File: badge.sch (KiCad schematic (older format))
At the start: 42 parts, among them U1 TPS61165

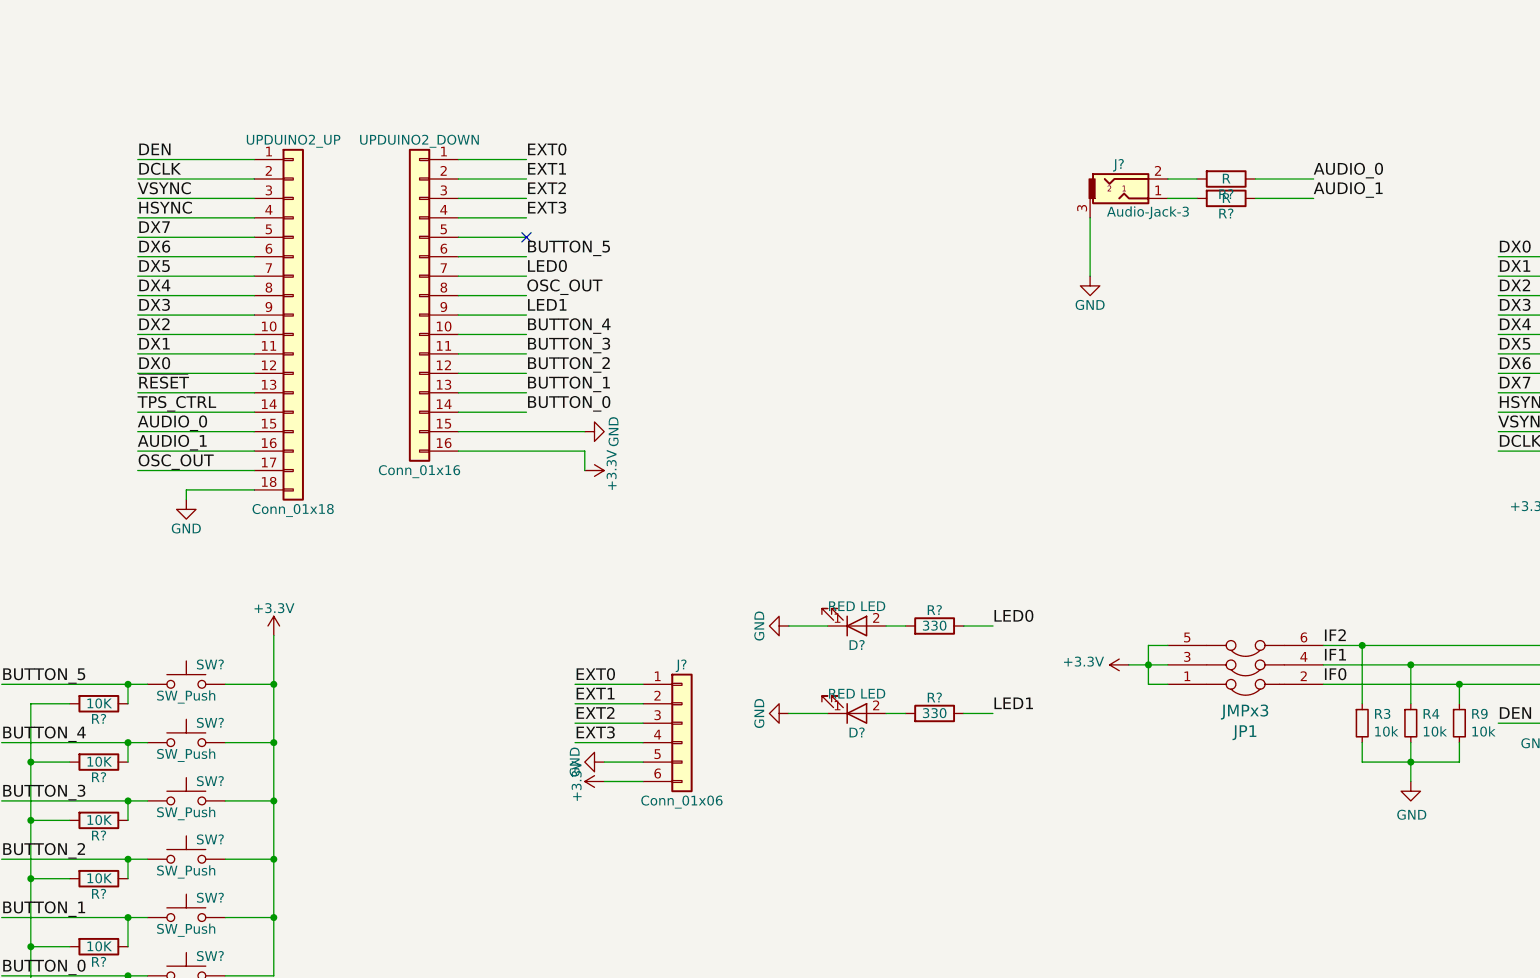
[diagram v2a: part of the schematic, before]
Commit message: Made audio mono and using pin 37, change port to PMOD, clk on proper pin,
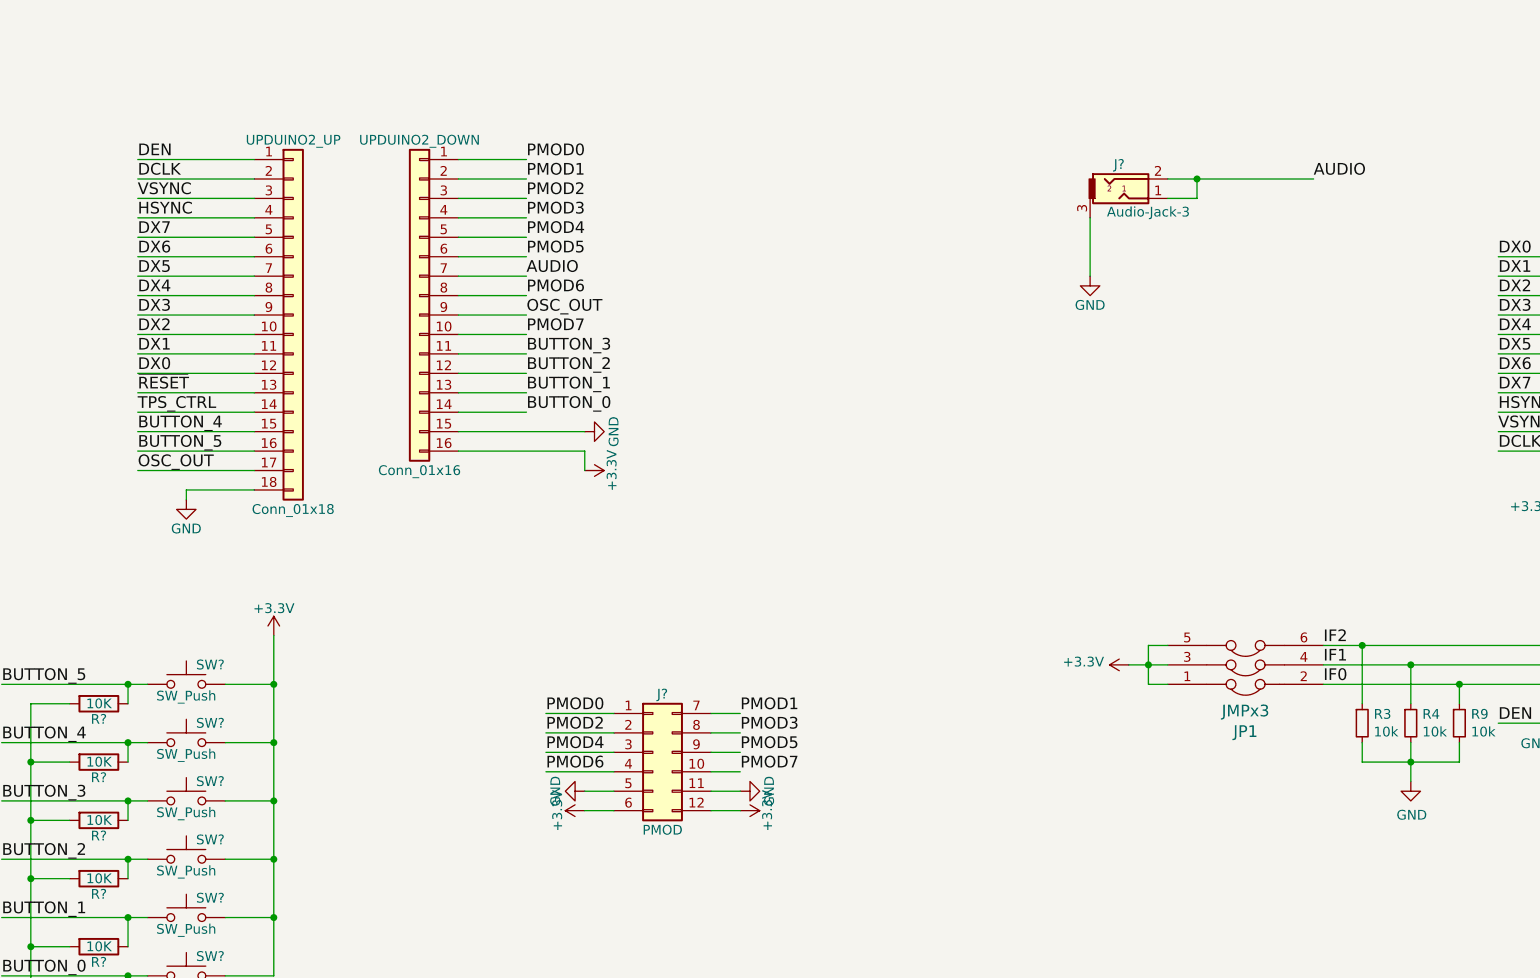
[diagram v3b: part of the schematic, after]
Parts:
- removed D? (x2): RED LED, symbol LED
- removed J?: Conn_01x06, symbol Conn_01x06
- removed R? (x2): R, symbol R
- removed R? (x2): 330, symbol R
- added J?: PMOD, symbol Conn_02x06_Top_Bottom
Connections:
- net AUDIO_0 is gone; now on net BUTTON_4: UPDUINO2_UP.15 (Pin_15)
- net AUDIO_1 is gone; now on net BUTTON_5: UPDUINO2_UP.16 (Pin_16)
- net LED0 is gone; now on net AUDIO: UPDUINO2_DOWN.7 (Pin_7)
- net LED1 is gone; now on net OSC_OUT: UPDUINO2_DOWN.9 (Pin_9)
- net +3V3: now also J?.12 (Pin_12), J?.6 (Pin_6)
- net BUTTON_4: no longer UPDUINO2_DOWN.10 (Pin_10)
- net BUTTON_5: no longer UPDUINO2_DOWN.6 (Pin_6)
- net GND: now also J?.11 (Pin_11), J?.5 (Pin_5)
- net OSC_OUT: no longer UPDUINO2_DOWN.8 (Pin_8)
- net PMOD4: now reaches UPDUINO2_DOWN.5 (Pin_5)
- net PMOD4: now also J?.3 (Pin_3)
- net AUDIO: now reaches J?.1
- net AUDIO: now also J?.2
- net EXT0 renamed PMOD0
- net PMOD0: now also J?.1 (Pin_1)
- net EXT1 renamed PMOD1
- net PMOD1: now also J?.7 (Pin_7)
- net EXT2 renamed PMOD2
- net PMOD2: now also J?.2 (Pin_2)
- net EXT3 renamed PMOD3
- net PMOD3: now also J?.8 (Pin_8)
- new net PMOD5: J?.9 (Pin_9), UPDUINO2_DOWN.6 (Pin_6)
- new net PMOD6: J?.4 (Pin_4), UPDUINO2_DOWN.8 (Pin_8)
- new net PMOD7: J?.10 (Pin_10), UPDUINO2_DOWN.10 (Pin_10)
- no-connect marks 12 -> 11
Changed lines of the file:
@@
 DEN
 Text Label 5900 6200 0    60   ~ 0
-AUDIO_1
+BUTTON_5
 Text Label 5900 6100 0    60   ~ 0
-AUDIO_0
+BUTTON_4
 Text Label 5900 6000 0    60   ~ 0
 TPS_CTRL
@@
 $EndComp
 Text Label 11950 4800 0    60   ~ 0
-AUDIO_0
+AUDIO
 Text Label 7900 4700 0    60   ~ 0
-EXT0
+PMOD0
 Text Label 7900 4800 0    60   ~ 0
-EXT1
-Text Label 11950 4900 0    60   ~ 0
-AUDIO_1
+PMOD1
 Text Label 7900 6000 0    60   ~ 0
 BUTTON_0
@@
 BUTTON_3
 Text Label 7900 5600 0    60   ~ 0
-BUTTON_4
+PMOD7
 $Comp
 L SW_Push SW?
@@
 $EndComp
 $Comp
-L R R?
-U 1 1 5A7F4132
-P 11500 4800
-F 0 "R?" V 11580 4800 50  0000 C CNN
-F 1 "R" V 11500 4800 50  0000 C CNN
-F 2 "" V 11430 4800 50  0001 C CNN
-F 3 "" H 11500 4800 50  0001 C CNN
-	1    11500 4800
-	0    1    1    0
-$EndComp
-$Comp
-L R R?
-U 1 1 5A7F41B1
-P 11500 4900
-F 0 "R?" V 11580 4900 50  0000 C CNN
-F 1 "R" V 11500 4900 50  0000 C CNN
-F 2 "" V 11430 4900 50  0001 C CNN
-F 3 "" H 11500 4900 50  0001 C CNN
-	1    11500 4900
-	0    1    1    0
-$EndComp
-$Comp
 L Audio-Jack-3 J?
 U 1 1 5A7F3EF2
@@
 	1    0    0    -1
 $EndComp
-Text Label 8150 7400 0    60   ~ 0
-EXT0
-Text Label 8150 7500 0    60   ~ 0
-EXT1
-Text Label 8150 7600 0    60   ~ 0
-EXT2
 Text Label 7900 4900 0    60   ~ 0
-EXT2
+PMOD2
 Text Label 7900 5000 0    60   ~ 0
-EXT3
-Text Label 7900 5200 0    60   ~ 0
-BUTTON_5
+PMOD3
 Text Label 7900 5400 0    60   ~ 0
-OSC_OUT
+PMOD6
 $Comp
 L GND #PWR?
@@
 	1    0    0    -1
 $EndComp
-$Comp
-L LED D?
-U 1 1 5A7FC771
-P 9600 7100
-F 0 "D?" H 9600 7200 50  0000 C CNN
-F 1 "RED LED" H 9600 7000 50  0000 C CNN
-F 2 "" H 9600 7100 50  0001 C CNN
-F 3 "" H 9600 7100 50  0001 C CNN
-	1    9600 7100
-	1    0    0    1
-$EndComp
-$Comp
-L R R?
-U 1 1 5A7FC9C8
-P 10000 7100
-F 0 "R?" V 10080 7100 50  0000 C CNN
-F 1 "330" V 10000 7100 50  0000 C CNN
-F 2 "" V 9930 7100 50  0001 C CNN
-F 3 "" H 10000 7100 50  0001 C CNN
-	1    10000 7100
-	0    1    -1   0
-$EndComp
-Text Label 10300 7100 0    60   ~ 0
-LED0
-$Comp
-L GND #PWR?
-U 1 1 5A7FCB50
-P 9250 7100
-F 0 "#PWR?" H 9250 6850 50  0001 C CNN
-F 1 "GND" H 9250 6950 50  0000 C CNN
-F 2 "" H 9250 7100 50  0001 C CNN
-F 3 "" H 9250 7100 50  0001 C CNN
-	1    9250 7100
-	0    1    -1   0
-$EndComp
 Wire Wire Line
 	6150 6400 6500 6400
@@
 	6150 6450 6150 6400
 Wire Wire Line
-	8150 7600 8500 7600
-Wire Wire Line
-	8150 7500 8500 7500
-Wire Wire Line
-	8150 7400 8500 7400
-Wire Wire Line
 	7550 5400 7900 5400
 Wire Wire Line
@@
 Wire Wire Line
 	7550 4900 7900 4900
-Wire Wire Line
-	11650 4900 11950 4900
 Wire Wire Line
 	11200 4900 11350 4900
@@
 Connection ~ 5850 8900
 Wire Wire Line
-	11200 4800 11350 4800
-Wire Wire Line
-	11650 4800 11950 4800
-Wire Wire Line
-	9450 7100 9250 7100
-Wire Wire Line
-	10300 7100 10150 7100
-Wire Wire Line
-	9850 7100 9750 7100
+	11200 4800 11950 4800
 $Comp
 L Conn_01x02 BATTERY
@@
 Wire Wire Line
 	6750 3600 6850 3600
-Text Label 8150 7700 0    60   ~ 0
-EXT3
-Wire Wire Line
-	8150 7700 8500 7700
-$Comp
-L Conn_01x06 J?
-U 1 1 5A7F0509
-P 8700 7600
-F 0 "J?" H 8700 7900 50  0000 C CNN
-F 1 "Conn_01x06" H 8700 7200 50  0000 C CNN
-F 2 "" H 8700 7600 50  0001 C CNN
-F 3 "" H 8700 7600 50  0001 C CNN
-	1    8700 7600
-	1    0    0    -1
-$EndComp
-$Comp
-L GND #PWR?
-U 1 1 5A7F0582
-P 8300 7800
-F 0 "#PWR?" H 8300 7550 50  0001 C CNN
-F 1 "GND" H 8300 7650 50  0000 C CNN
-F 2 "" H 8300 7800 50  0001 C CNN
-F 3 "" H 8300 7800 50  0001 C CNN
-	1    8300 7800
-	0    1    1    0
-$EndComp
-$Comp
-L +3.3V #PWR?
-U 1 1 5A7F0636
-P 8300 7900
-F 0 "#PWR?" H 8300 7750 50  0001 C CNN
-F 1 "+3.3V" H 8300 8040 50  0000 C CNN
-F 2 "" H 8300 7900 50  0001 C CNN
-F 3 "" H 8300 7900 50  0001 C CNN
-	1    8300 7900
-	0    -1   -1   0
-$EndComp
-Wire Wire Line
-	8300 7800 8500 7800
-Wire Wire Line
-	8300 7900 8500 7900
 Wire Wire Line
 	13450 3300 12800 3300
@@
 Wire Wire Line
 	13450 3500 12800 3500
-Text Label 7900 5300 0    60   ~ 0
-LED0
 Text Label 7900 5500 0    60   ~ 0
-LED1
+OSC_OUT
 Wire Wire Line
 	7900 5300 7550 5300
 Wire Wire Line
 	7900 5500 7550 5500
-$Comp
-L LED D?
-U 1 1 5A7F8496
-P 9600 7550
-F 0 "D?" H 9600 7650 50  0000 C CNN
-F 1 "RED LED" H 9600 7450 50  0000 C CNN
-F 2 "" H 9600 7550 50  0001 C CNN
-F 3 "" H 9600 7550 50  0001 C CNN
-	1    9600 7550
-	1    0    0    1
-$EndComp
-$Comp
-L R R?
-U 1 1 5A7F849C
-P 10000 7550
-F 0 "R?" V 10080 7550 50  0000 C CNN
-F 1 "330" V 10000 7550 50  0000 C CNN
-F 2 "" V 9930 7550 50  0001 C CNN
-F 3 "" H 10000 7550 50  0001 C CNN
-	1    10000 7550
-	0    1    -1   0
-$EndComp
-Text Label 10300 7550 0    60   ~ 0
-LED1
-$Comp
-L GND #PWR?
-U 1 1 5A7F84A3
-P 9250 7550
-F 0 "#PWR?" H 9250 7300 50  0001 C CNN
-F 1 "GND" H 9250 7400 50  0000 C CNN
-F 2 "" H 9250 7550 50  0001 C CNN
-F 3 "" H 9250 7550 50  0001 C CNN
-	1    9250 7550
-	0    1    -1   0
-$EndComp
-Wire Wire Line
-	9450 7550 9250 7550
-Wire Wire Line
-	10300 7550 10150 7550
-Wire Wire Line
-	9850 7550 9750 7550
 Text Label 8750 1800 0    60   ~ 0
 TPS_CTRL
@@
 	8450 1800 8450 1600
 Connection ~ 8450 1600
-NoConn ~ 7900 5100
 NoConn ~ 7250 3700
+Text Label 7900 5100 0    60   ~ 0
+PMOD4
+Text Label 7900 5200 0    60   ~ 0
+PMOD5
+Text Label 7900 5300 0    60   ~ 0
+AUDIO
+Wire Wire Line
+	11350 4900 11350 4800
+Connection ~ 11350 4800
+$Comp
+L Conn_02x06_Top_Bottom J?
+U 1 1 5A7F4E92
+P 8550 7750
+F 0 "J?" H 8600 8050 50  0000 C CNN
+F 1 "PMOD" H 8600 7350 50  0000 C CNN
+F 2 "" H 8550 7750 50  0001 C CNN
+F 3 "" H 8550 7750 50  0001 C CNN
+	1    8550 7750
+	1    0    0    -1
+$EndComp
+$Comp
+L GND #PWR?
+U 1 1 5A7F4F71
+P 8200 7950
+F 0 "#PWR?" H 8200 7700 50  0001 C CNN
+F 1 "GND" H 8200 7800 50  0000 C CNN
+F 2 "" H 8200 7950 50  0001 C CNN
+F 3 "" H 8200 7950 50  0001 C CNN
+	1    8200 7950
+	0    1    1    0
+$EndComp
+$Comp
+L GND #PWR?
+U 1 1 5A7F501C
+P 9000 7950
+F 0 "#PWR?" H 9000 7700 50  0001 C CNN
+F 1 "GND" H 9000 7800 50  0000 C CNN
+F 2 "" H 9000 7950 50  0001 C CNN
+F 3 "" H 9000 7950 50  0001 C CNN
+	1    9000 7950
+	0    -1   -1   0
+$EndComp
+$Comp
+L +3.3V #PWR?
+U 1 1 5A7F5078
+P 8200 8050
+F 0 "#PWR?" H 8200 7900 50  0001 C CNN
+F 1 "+3.3V" H 8200 8190 50  0000 C CNN
+F 2 "" H 8200 8050 50  0001 C CNN
+F 3 "" H 8200 8050 50  0001 C CNN
+	1    8200 8050
+	0    -1   -1   0
+$EndComp
+$Comp
+L +3.3V #PWR?
+U 1 1 5A7F514A
+P 9000 8050
+F 0 "#PWR?" H 9000 7900 50  0001 C CNN
+F 1 "+3.3V" H 9000 8190 50  0000 C CNN
+F 2 "" H 9000 8050 50  0001 C CNN
+F 3 "" H 9000 8050 50  0001 C CNN
+	1    9000 8050
+	0    1    1    0
+$EndComp
+Wire Wire Line
+	9000 8050 8850 8050
+Wire Wire Line
+	8350 7950 8200 7950
+Wire Wire Line
+	8350 8050 8200 8050
+Wire Wire Line
+	8850 7950 9000 7950
+Text Label 8000 7550 0    60   ~ 0
+PMOD0
+Text Label 8000 7650 0    60   ~ 0
+PMOD2
+Text Label 8000 7750 0    60   ~ 0
+PMOD4
+Text Label 8000 7850 0    60   ~ 0
+PMOD6
+Text Label 9000 7550 0    60   ~ 0
+PMOD1
+Text Label 9000 7650 0    60   ~ 0
+PMOD3
+Text Label 9000 7750 0    60   ~ 0
+PMOD5
+Text Label 9000 7850 0    60   ~ 0
+PMOD7
+Wire Wire Line
+	9000 7550 8850 7550
+Wire Wire Line
+	9000 7650 8850 7650
+Wire Wire Line
+	9000 7750 8850 7750
+Wire Wire Line
+	9000 7850 8850 7850
+Wire Wire Line
+	8000 7550 8350 7550
+Wire Wire Line
+	8000 7650 8350 7650
+Wire Wire Line
+	8000 7750 8350 7750
+Wire Wire Line
+	8000 7850 8350 7850
 $EndSCHEMATC

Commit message: Footprint assignments and initial placement
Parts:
- removed JP1: JMPx3, Pin_Headers:Pin_Header_Straight_2x03_Pitch2.54mm, symbol JMPx3
- added J3, J4: HOLE, Mounting_Holes:MountingHole_3.2mm_M3, symbol Conn_01x01
- added R16, R17: DNP, Resistors_SMD:R_0603, symbol R_Small
- added R18: 10k, Resistors_SMD:R_0603, symbol R_Small
- BATTERY1: renamed from BATTERY; footprint (none) -> Pin_Headers:Pin_Header_Straight_1x02_Pitch2.54mm
- J1: renamed from J?; footprint (none) -> Custom Parts:Pin_Header_Angled_2x06_Pitch2.54mm_PMOD
- J2: renamed from J?; footprint (none) -> Custom Parts:AUDIO_JACK_3.5mm
- R10, R11, R12, R13, R14, R15: renamed from R?; footprint (none) -> Resistors_SMD:R_0603
- R9: value 10k -> DNP
- SW1, SW2, SW3, SW4, SW5, SW6: renamed from SW?; footprint (none) -> Buttons_Switches_THT:SW_PUSH-12mm
- SW7: renamed from SW?; footprint (none) -> Buttons_Switches_THT:SW_CuK_OS102011MA1QN1_SPDT_Angled
- UPDUINO2_DOWN1: renamed from UPDUINO2_DOWN; footprint (none) -> Pin_Headers:Pin_Header_Straight_1x16_Pitch2.54mm
- UPDUINO2_UP1: renamed from UPDUINO2_UP; footprint (none) -> Pin_Headers:Pin_Header_Straight_1x18_Pitch2.54mm
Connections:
- net +3V3: now also R16.2, R17.2, R18.2
- net DCLK: now also UPDUINO2_UP1.12 (Pin_12); no longer UPDUINO2_UP1.2 (Pin_2)
- net DEN: now also UPDUINO2_UP1.13 (Pin_13); no longer UPDUINO2_UP1.1 (Pin_1)
- net DX0: now also UPDUINO2_UP1.2 (Pin_2); no longer UPDUINO2_UP1.12 (Pin_12)
- net DX1: now also UPDUINO2_UP1.3 (Pin_3); no longer UPDUINO2_UP1.11 (Pin_11)
- net DX2: now also UPDUINO2_UP1.4 (Pin_4); no longer UPDUINO2_UP1.10 (Pin_10)
- net DX3: now also UPDUINO2_UP1.5 (Pin_5); no longer UPDUINO2_UP1.9 (Pin_9)
- net DX4: now also UPDUINO2_UP1.6 (Pin_6); no longer UPDUINO2_UP1.8 (Pin_8)
- net DX6: now also UPDUINO2_UP1.8 (Pin_8); no longer UPDUINO2_UP1.6 (Pin_6)
- net DX7: now also UPDUINO2_UP1.9 (Pin_9); no longer UPDUINO2_UP1.5 (Pin_5)
- net HSYNC: now also UPDUINO2_UP1.10 (Pin_10); no longer UPDUINO2_UP1.4 (Pin_4)
- net IF0: now also R18.1
- net IF1: now also R17.1
- net IF2: now also R16.1
- net PMOD0: now also UPDUINO2_DOWN1.10 (Pin_10); no longer UPDUINO2_DOWN1.1 (Pin_1)
- net PMOD1: now also UPDUINO2_DOWN1.8 (Pin_8); no longer UPDUINO2_DOWN1.2 (Pin_2)
- net PMOD2: now also UPDUINO2_DOWN1.6 (Pin_6); no longer UPDUINO2_DOWN1.3 (Pin_3)
- net PMOD3: now also UPDUINO2_DOWN1.5 (Pin_5); no longer UPDUINO2_DOWN1.4 (Pin_4)
- net PMOD4: now also UPDUINO2_DOWN1.4 (Pin_4); no longer UPDUINO2_DOWN1.5 (Pin_5)
- net PMOD5: now also UPDUINO2_DOWN1.3 (Pin_3); no longer UPDUINO2_DOWN1.6 (Pin_6)
- net PMOD6: now also UPDUINO2_DOWN1.2 (Pin_2); no longer UPDUINO2_DOWN1.8 (Pin_8)
- net PMOD7: now also UPDUINO2_DOWN1.1 (Pin_1); no longer UPDUINO2_DOWN1.10 (Pin_10)
- net VSYNC: now also UPDUINO2_UP1.11 (Pin_11); no longer UPDUINO2_UP1.3 (Pin_3)
- net ~RESET: now also UPDUINO2_UP1.1 (Pin_1); no longer UPDUINO2_UP1.13 (Pin_13)
- no-connect marks 11 -> 13

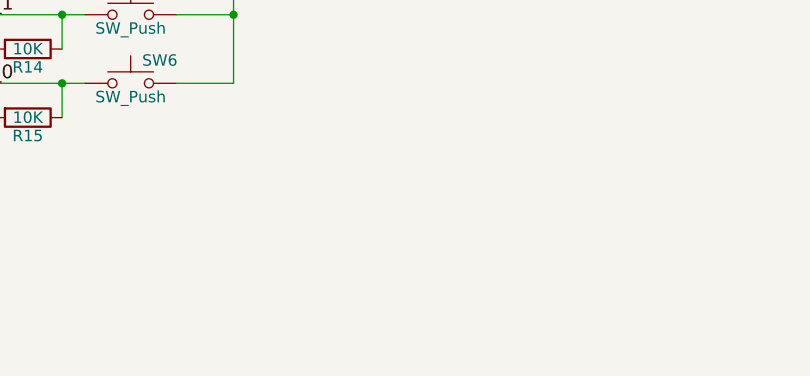
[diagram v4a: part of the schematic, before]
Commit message: Routing done and logos added
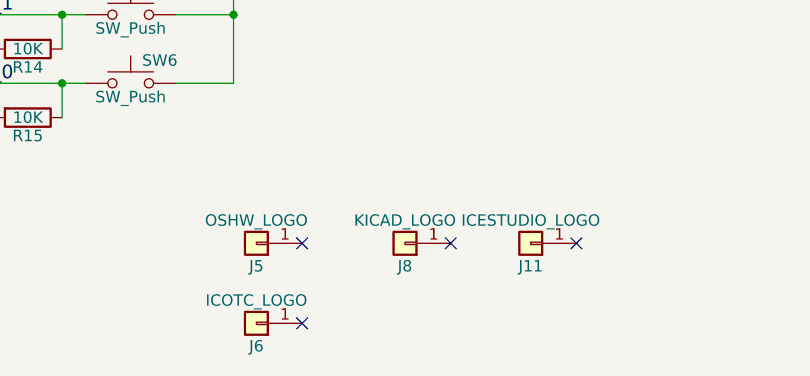
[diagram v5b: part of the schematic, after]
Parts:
- added J11: ICESTUDIO_LOGO, Custom Parts:ICESTUDIO, symbol Conn_01x01
- added J5: OSHW_LOGO, Symbols:OSHW-Logo2_24.3x20mm_SilkScreen, symbol Conn_01x01
- added J6: ICOTC_LOGO, Custom Parts:ICOTC, symbol Conn_01x01
- added J8: KICAD_LOGO, Symbols:KiCad-Logo_12mm_SilkScreen, symbol Conn_01x01
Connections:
- no-connect marks 13 -> 17
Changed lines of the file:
@@
 NoConn ~ 6350 2600
 NoConn ~ 6350 2900
+$Comp
+L Conn_01x01 J5
+U 1 1 5A80235E
+P 6700 9600
+F 0 "J5" H 6700 9700 50  0000 C CNN
+F 1 "OSHW_LOGO" H 6700 9500 50  0000 C CNN
+F 2 "Symbols:OSHW-Logo2_24.3x20mm_SilkScreen" H 6700 9600 50  0001 C CNN
+F 3 "" H 6700 9600 50  0001 C CNN
+	1    6700 9600
+	-1   0    0    1
+$EndComp
+NoConn ~ 6900 9600
+$Comp
+L Conn_01x01 J6
+U 1 1 5A802842
+P 6700 9950
+F 0 "J6" H 6700 10050 50  0000 C CNN
+F 1 "ICOTC_LOGO" H 6700 9850 50  0000 C CNN
+F 2 "Custom Parts:ICOTC" H 6700 9950 50  0001 C CNN
+F 3 "" H 6700 9950 50  0001 C CNN
+	1    6700 9950
+	-1   0    0    1
+$EndComp
+$Comp
+L Conn_01x01 J8
+U 1 1 5A802C1B
+P 7350 9600
+F 0 "J8" H 7350 9700 50  0000 C CNN
+F 1 "KICAD_LOGO" H 7350 9500 50  0000 C CNN
+F 2 "Symbols:KiCad-Logo_12mm_SilkScreen" H 7350 9600 50  0001 C CNN
+F 3 "" H 7350 9600 50  0001 C CNN
+	1    7350 9600
+	-1   0    0    1
+$EndComp
+NoConn ~ 7550 9600
+NoConn ~ 6900 9950
+$Comp
+L Conn_01x01 J11
+U 1 1 5A8032EC
+P 7900 9600
+F 0 "J11" H 7900 9700 50  0000 C CNN
+F 1 "ICESTUDIO_LOGO" H 7900 9500 50  0000 C CNN
+F 2 "Custom Parts:ICESTUDIO" H 7900 9600 50  0001 C CNN
+F 3 "" H 7900 9600 50  0001 C CNN
+	1    7900 9600
+	-1   0    0    1
+$EndComp
+NoConn ~ 8100 9600
 $EndSCHEMATC

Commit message: Final tweaks, create gerbers
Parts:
- added J7: OSHPARK_LOGO, Custom Parts:OSHPARK, symbol Conn_01x01
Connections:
- no-connect marks 17 -> 20
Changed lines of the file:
@@
 $EndComp
 NoConn ~ 8100 9600
+$Comp
+L Conn_01x01 J7
+U 1 1 5A81D496
+P 7350 9950
+F 0 "J7" H 7350 10050 50  0000 C CNN
+F 1 "OSHPARK_LOGO" H 7350 9850 50  0000 C CNN
+F 2 "Custom Parts:OSHPARK" H 7350 9950 50  0001 C CNN
+F 3 "" H 7350 9950 50  0001 C CNN
+	1    7350 9950
+	-1   0    0    1
+$EndComp
+NoConn ~ 7550 9950
+NoConn ~ 7900 3500
+NoConn ~ 7700 9800
 $EndSCHEMATC
